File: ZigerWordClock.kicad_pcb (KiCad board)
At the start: 2 copper layers, 237 x 237 mm, 106 parts, among them J1 SAO 1.69bis, J2 Barrel_Jack, U1 BH1750, U10 BTF-5V-060L-B_SK9822_LED_Stri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, U11 BTF-5V-060L-B_SK9822_LED_Stri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, U12 BTF-5V-060L-B_SK9822_LED_Stri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, U13 BTF-5V-060L-B_SK9822_LED_Stri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, U14 BTF-5V-060L-B_SK9822_LED_Stri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, U15 BTF-5V-060L-B_SK9822_LED_Stri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, U16 BTF-5V-060L-B_SK9822_LED_Stri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, U17 BTF-5V-060L-B_SK9822_LED_Stri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, U18 BTF-5V-060L-B_SK9822_LED_Stri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, U19 BTF-5V-060L-B_SK9822_LED_Stri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, U2 LILYGO(R)_TTGO_T8_ESP32-S2_V1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, U20 IR-Module_38KHz, U3 BTF-5V-060L-B_SK9822_LED_Stri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, U4 LevelShifter, U5 BTF-5V-060L-B_SK9822_LED_Stri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, U6 BTF-5V-060L-B_SK9822_LED_Stri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, U7 BTF-5V-060L-B_SK9822_LED_Stri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, U8 BTF-5V-060L-B_SK9822_LED_Stri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, U9 BTF-5V-060L-B_SK9822_LED_Stri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

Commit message: Added silkscreen graphics and version number
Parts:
- added G***: LOGO, WordClock Footprint Library:QR Code ZigerWordClock PCB, B.Cu at (250.7, 59.2)
- added G1: LOGO, WordClock Footprint Library:Schriftzug MiZ, F.Cu at (269.2, 149.6)
- added G2: LOGO, WordClock Footprint Library:Schriftzug Wordclock, F.Cu at (51.6, 149.1)
- added G3: LOGO, WordClock Footprint Library:BackLogo, B.Cu at (153.0, 152.7)
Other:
- board text added: "Infrared Module"
- board text added: "Light Sensor"
- board text added: "Version 1.0"
- board text added: "WiFi LED"

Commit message: Add mounting holes, moved barrel jack, adjusted graphics
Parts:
- added REF**: MountingHole_3.2mm_M3, MountingHole:MountingHole_3.2mm_M3, F.Cu at (274.1, 35.8)
- added REF**: MountingHole_3.2mm_M3, MountingHole:MountingHole_3.2mm_M3, F.Cu at (46.5, 35.8)
- added REF**: MountingHole_3.2mm_M3, MountingHole:MountingHole_3.2mm_M3, F.Cu at (274.6, 263.7)
- added REF**: MountingHole_3.2mm_M3, MountingHole:MountingHole_3.2mm_M3, F.Cu at (46.5, 263.4)
- added REF**: MountingHole_3.2mm_M3, MountingHole:MountingHole_3.2mm_M3, F.Cu at (168.7, 166.4)
- moved J2 31.7 mm to (77.0, 250.9)
- moved G*** 6.47 mm to (246.1, 63.8)
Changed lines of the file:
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@@
     )
   )
-  (footprint "WordClock Footprint Library:Schriftzug Wordclock" (layer "F.Cu")
+  (footprint "MountingHole:MountingHole_3.2mm_M3" locked (layer "F.Cu")
+    (at 274.066 35.814)
+    (descr "Mounting Hole 3.2mm, no annular, M3")
+    (tags "mounting hole 3.2mm no annular m3")
+    (attr exclude_from_pos_files exclude_from_bom)
+    (fp_text reference "REF**" (at 0 -4.2) (layer "F.SilkS") hide
+      (effects (font (size 1 1) (thickness 0.15)))
+    )
+    (fp_text value "MountingHole_3.2mm_M3" (at 0 4.2) (layer "F.Fab")
+      (effects (font (size 1 1) (thickness 0.15)))
+    )
+    (fp_text user "${REFERENCE}" (at 0.3 0) (layer "F.Fab")
+      (effects (font (size 1 1) (thickness 0.15)))
+    )
+    (fp_circle (center 0 0) (end 3.2 0) (layer "Cmts.User") (width 0.15) (fill none))
+    (fp_circle (center 0 0) (end 3.45 0) (layer "F.CrtYd") (width 0.05) (fill none))
+    (pad "" np_thru_hole circle locked (at 0 0) (size 3.2 3.2) (drill 3.2) (layers *.Cu *.Mask))
+  )
+  (footprint "MountingHole:MountingHole_3.2mm_M3" (layer "F.Cu")
+    (at 46.482 35.814)
+    (descr "Mounting Hole 3.2mm, no annular, M3")
+    (tags "mounting hole 3.2mm no annular m3")
+    (attr exclude_from_pos_files exclude_from_bom)
+    (fp_text reference "REF**" (at 0 -4.2) (layer "F.SilkS") hide
+      (effects (font (size 1 1) (thickness 0.15)))
+    )
+    (fp_text value "MountingHole_3.2mm_M3" (at 0 4.2) (layer "F.Fab")
+      (effects (font (size 1 1) (thickness 0.15)))
+    )
+    (fp_text user "${REFERENCE}" (at 0.3 0) (layer "F.Fab")
+      (effects (font (size 1 1) (thickness 0.15)))
+    )
+    (fp_circle (center 0 0) (end 3.2 0) (layer "Cmts.User") (width 0.15) (fill none))
+    (fp_circle (center 0 0) (end 3.45 0) (layer "F.CrtYd") (width 0.05) (fill none))
+    (pad "" np_thru_hole circle locked (at 0 0) (size 3.2 3.2) (drill 3.2) (layers *.Cu *.Mask))
+  )
+  (footprint "WordClock Footprint Library:Schriftzug Wordclock" locked (layer "F.Cu")
     (at 51.562 149.098 -90)
     (attr board_only exclude_from_pos_files exclude_from_bom)
@@
     )
   )
+  (footprint "MountingHole:MountingHole_3.2mm_M3" locked (layer "F.Cu")
+    (at 274.574 263.652)
+    (descr "Mounting Hole 3.2mm, no annular, M3")
+    (tags "mounting hole 3.2mm no annular m3")
+    (attr exclude_from_pos_files exclude_from_bom)
+    (fp_text reference "REF**" (at 0 -4.2) (layer "F.SilkS") hide
+      (effects (font (size 1 1) (thickness 0.15)))
+    )
+    (fp_text value "MountingHole_3.2mm_M3" (at 0 4.2) (layer "F.Fab")
+      (effects (font (size 1 1) (thickness 0.15)))
+    )
+    (fp_text user "${REFERENCE}" (at 0.3 0) (layer "F.Fab")
+      (effects (font (size 1 1) (thickness 0.15)))
+    )
+    (fp_circle (center 0 0) (end 3.2 0) (layer "Cmts.User") (width 0.15) (fill none))
+    (fp_circle (center 0 0) (end 3.45 0) (layer "F.CrtYd") (width 0.05) (fill none))
+    (pad "" np_thru_hole circle locked (at 0 0) (size 3.2 3.2) (drill 3.2) (layers *.Cu *.Mask))
+  )
   (footprint "WordClock Footprint Library:BTF-5V-060L-B SK9822 LED Strip - 11 Segment" locked (layer "F.Cu")
     (at 160.1886 149.5213 180)
@@
     )
   )
+  (footprint "MountingHole:MountingHole_3.2mm_M3" locked (layer "F.Cu")
+    (at 46.482 263.398)
+    (descr "Mounting Hole 3.2mm, no annular, M3")
+    (tags "mounting hole 3.2mm no annular m3")
+    (attr exclude_from_pos_files exclude_from_bom)
+    (fp_text reference "REF**" (at 0 -4.2) (layer "F.SilkS") hide
+      (effects (font (size 1 1) (thickness 0.15)))
+    )
+    (fp_text value "MountingHole_3.2mm_M3" (at 0 4.2) (layer "F.Fab")
+      (effects (font (size 1 1) (thickness 0.15)))
+    )
+    (fp_text user "${REFERENCE}" (at 0.3 0) (layer "F.Fab")
+      (effects (font (size 1 1) (thickness 0.15)))
+    )
+    (fp_circle (center 0 0) (end 3.2 0) (layer "Cmts.User") (width 0.15) (fill none))
+    (fp_circle (center 0 0) (end 3.45 0) (layer "F.CrtYd") (width 0.05) (fill none))
+    (pad "" np_thru_hole circle locked (at 0 0) (size 3.2 3.2) (drill 3.2) (layers *.Cu *.Mask))
+  )
   (footprint "WordClock Footprint Library:BH1750 Breakout Board" locked (layer "F.Cu")
     (at 160.058654 257.18123)
@@
     )
   )
-  (footprint "WordClock Footprint Library:Schriftzug MiZ" (layer "F.Cu")
+  (footprint "WordClock Footprint Library:Schriftzug MiZ" locked (layer "F.Cu")
     (at 269.24 149.606 90)
     (attr board_only exclude_from_pos_files exclude_from_bom)
@@
       ) (layer "F.SilkS") (width 0) (fill solid))
   )
+  (footprint "MountingHole:MountingHole_3.2mm_M3" (layer "F.Cu")
+    (at 168.656 166.36404)
+    (descr "Mounting Hole 3.2mm, no annular, M3")
+    (tags "mounting hole 3.2mm no annular m3")
+    (attr exclude_from_pos_files exclude_from_bom)
+    (fp_text reference "REF**" (at 0 -4.2) (layer "F.SilkS") hide
+      (effects (font (size 1 1) (thickness 0.15)))
+    )
+    (fp_text value "MountingHole_3.2mm_M3" (at 0 4.2) (layer "F.Fab")
+      (effects (font (size 1 1) (thickness 0.15)))
+    )
+    (fp_text user "${REFERENCE}" (at 0.3 0) (layer "F.Fab")
+      (effects (font (size 1 1) (thickness 0.15)))
+    )
+    (fp_circle (center 0 0) (end 3.2 0) (layer "Cmts.User") (width 0.15) (fill none))
+    (fp_circle (center 0 0) (end 3.45 0) (layer "F.CrtYd") (width 0.05) (fill none))
+    (pad "" np_thru_hole circle (at 0 0) (size 3.2 3.2) (drill 3.2) (layers *.Cu *.Mask))
+  )
   (footprint "WordClock Footprint Library:BTF-5V-060L-B SK9822 LED Strip - 11 Segment" locked (layer "F.Cu")
     (at 160.1886 166.36404)
@@
       (net 57 "Net-(JP20-Pad1)") (pinfunction "1") (pintype "passive"))
   )
-  (footprint "WordClock Footprint Library:QR Code ZigerWordClock PCB" (layer "B.Cu")
-    (at 250.698 59.182 180)
+  (footprint "WordClock Footprint Library:QR Code ZigerWordClock PCB" locked (layer "B.Cu")
+    (at 246.126 63.754 180)
     (attr board_only exclude_from_pos_files exclude_from_bom)
     (fp_text reference "G***" (at 0 0) (layer "B.SilkS") hide
@@
       ) (layer "B.SilkS") (width 0) (fill solid))
   )
-  (footprint "WordClock Footprint Library:BackLogo" (layer "B.Cu")
+  (footprint "WordClock Footprint Library:BackLogo" locked (layer "B.Cu")
     (at 153.037186 152.72006 180)
     (attr board_only exclude_from_pos_files exclude_from_bom)
@@
       (primitives
         (gr_poly (pts
-            (xy 0.55 -0.75)
-            (xy 0 -0.75)
-            (xy 0 0.75)
             (xy 0.55 0.75)
+            (xy 0 0.75)
+            (xy 0 -0.75)
+            (xy 0.55 -0.75)
           ) (width 0) (fill yes))
             (gr_circle (center 0 -0.25) (end 0.5 -0.25) (width 0) (fill yes))
@@
         (gr_circle (center 0 0.25) (end 0.5 0.25) (width 0) (fill yes))
         (gr_poly (pts
-            (xy 0 -0.75)
-            (xy -0.55 -0.75)
-            (xy -0.55 0.75)
             (xy 0 0.75)
+            (xy -0.55 0.75)
+            (xy -0.55 -0.75)
+            (xy 0 -0.75)
           ) (width 0) (fill yes))
       ))
@@
   )
   (footprint "Connector_PinHeader_2.54mm:PinHeader_1x02_P2.54mm_Vertical" (layer "B.Cu")
-    (at 47 261.225 180)
+    (at 76.962 250.947 180)
     (descr "Through hole straight pin header, 1x02, 2.54mm pitch, single row")
     (tags "Through hole pin header THT 1x02 2.54mm single row")
@@
       (net 58 "Net-(JP23-Pad1)") (pinfunction "1") (pintype "passive"))
   )
-  (gr_rect (start 34.544 271.272) (end 65.532 245.872) (layer "B.SilkS") (width 0.2) (fill solid))
+  (gr_rect locked (start 34.544 271.272) (end 65.532 245.872) (layer "B.SilkS") (width 0.2) (fill solid))
   (gr_poly
     (pts
@@
       (xy 41.837005 31.032291)
     ) (layer "Edge.Cuts") (width 0.1) (fill none))
-  (gr_text "Infrared Module" (at 118.11 259.842) (layer "F.Cu")
-    (effects (font (size 1.5 1.5) (thickness 0.3)))
-  )
-  (gr_text "Light Sensor" (at 160.02 245.872) (layer "F.Cu")
+  (gr_text "Infrared Module" (at 118.11 259.842) (layer "F.SilkS")
     (effects (font (size 1.5 1.5) (thickness 0.3)))
   )
@@
     (effects (font (size 1.5 1.5) (thickness 0.3)))
   )
+  (gr_text "Light Sensor" (at 160.02 245.872) (layer "F.SilkS")
+    (effects (font (size 1.5 1.5) (thickness 0.3)))
+  )

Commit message: Added JLCPCB DRC Rules
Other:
- rule pad_to_mask_clearance: 0 -> 0.05
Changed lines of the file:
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@@
       (dielectric_constraints no)
     )
-    (pad_to_mask_clearance 0)
+    (pad_to_mask_clearance 0.05)
+    (solder_mask_min_width 0.254)
     (pcbplotparams
       (layerselection 0x00010fc_ffffffff)

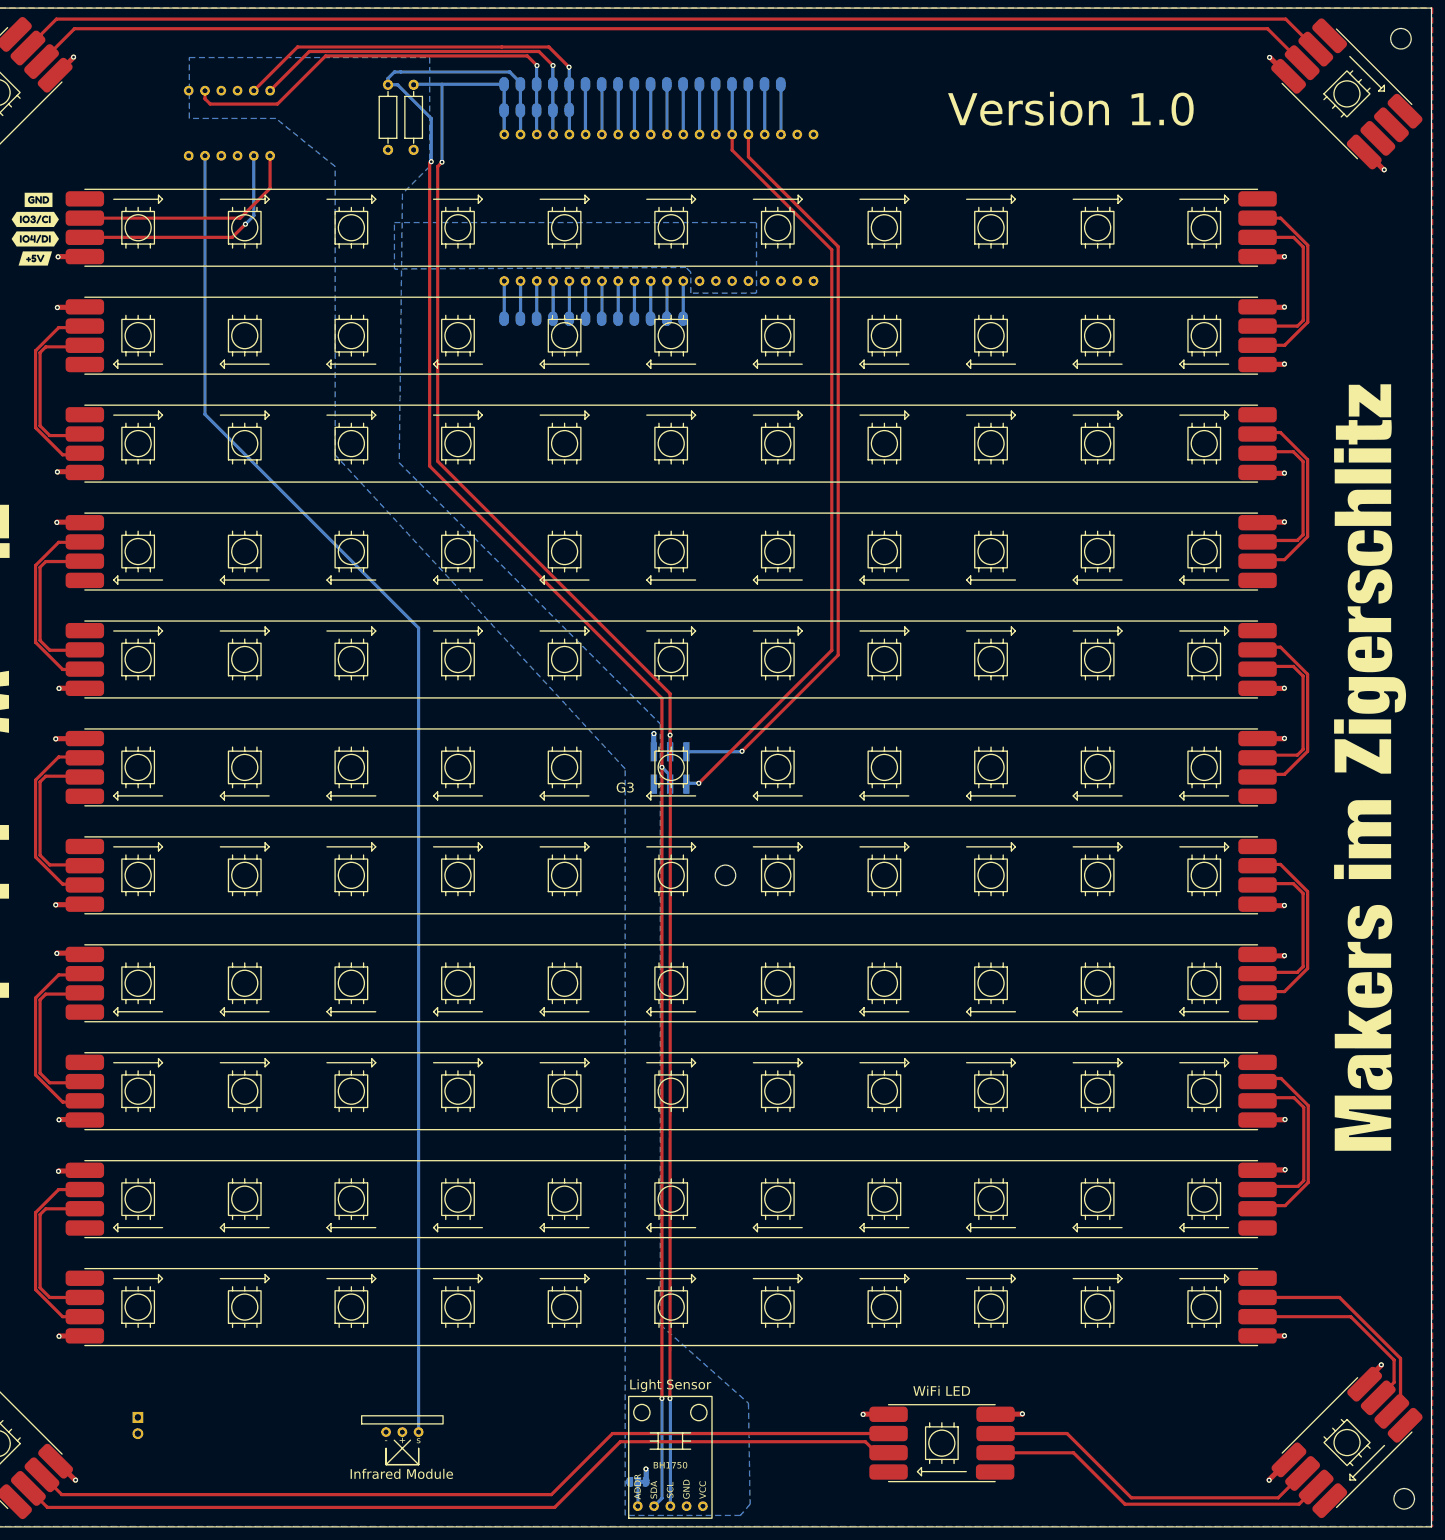
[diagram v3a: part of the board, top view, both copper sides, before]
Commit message: Moved copper traces and created GERBER Files
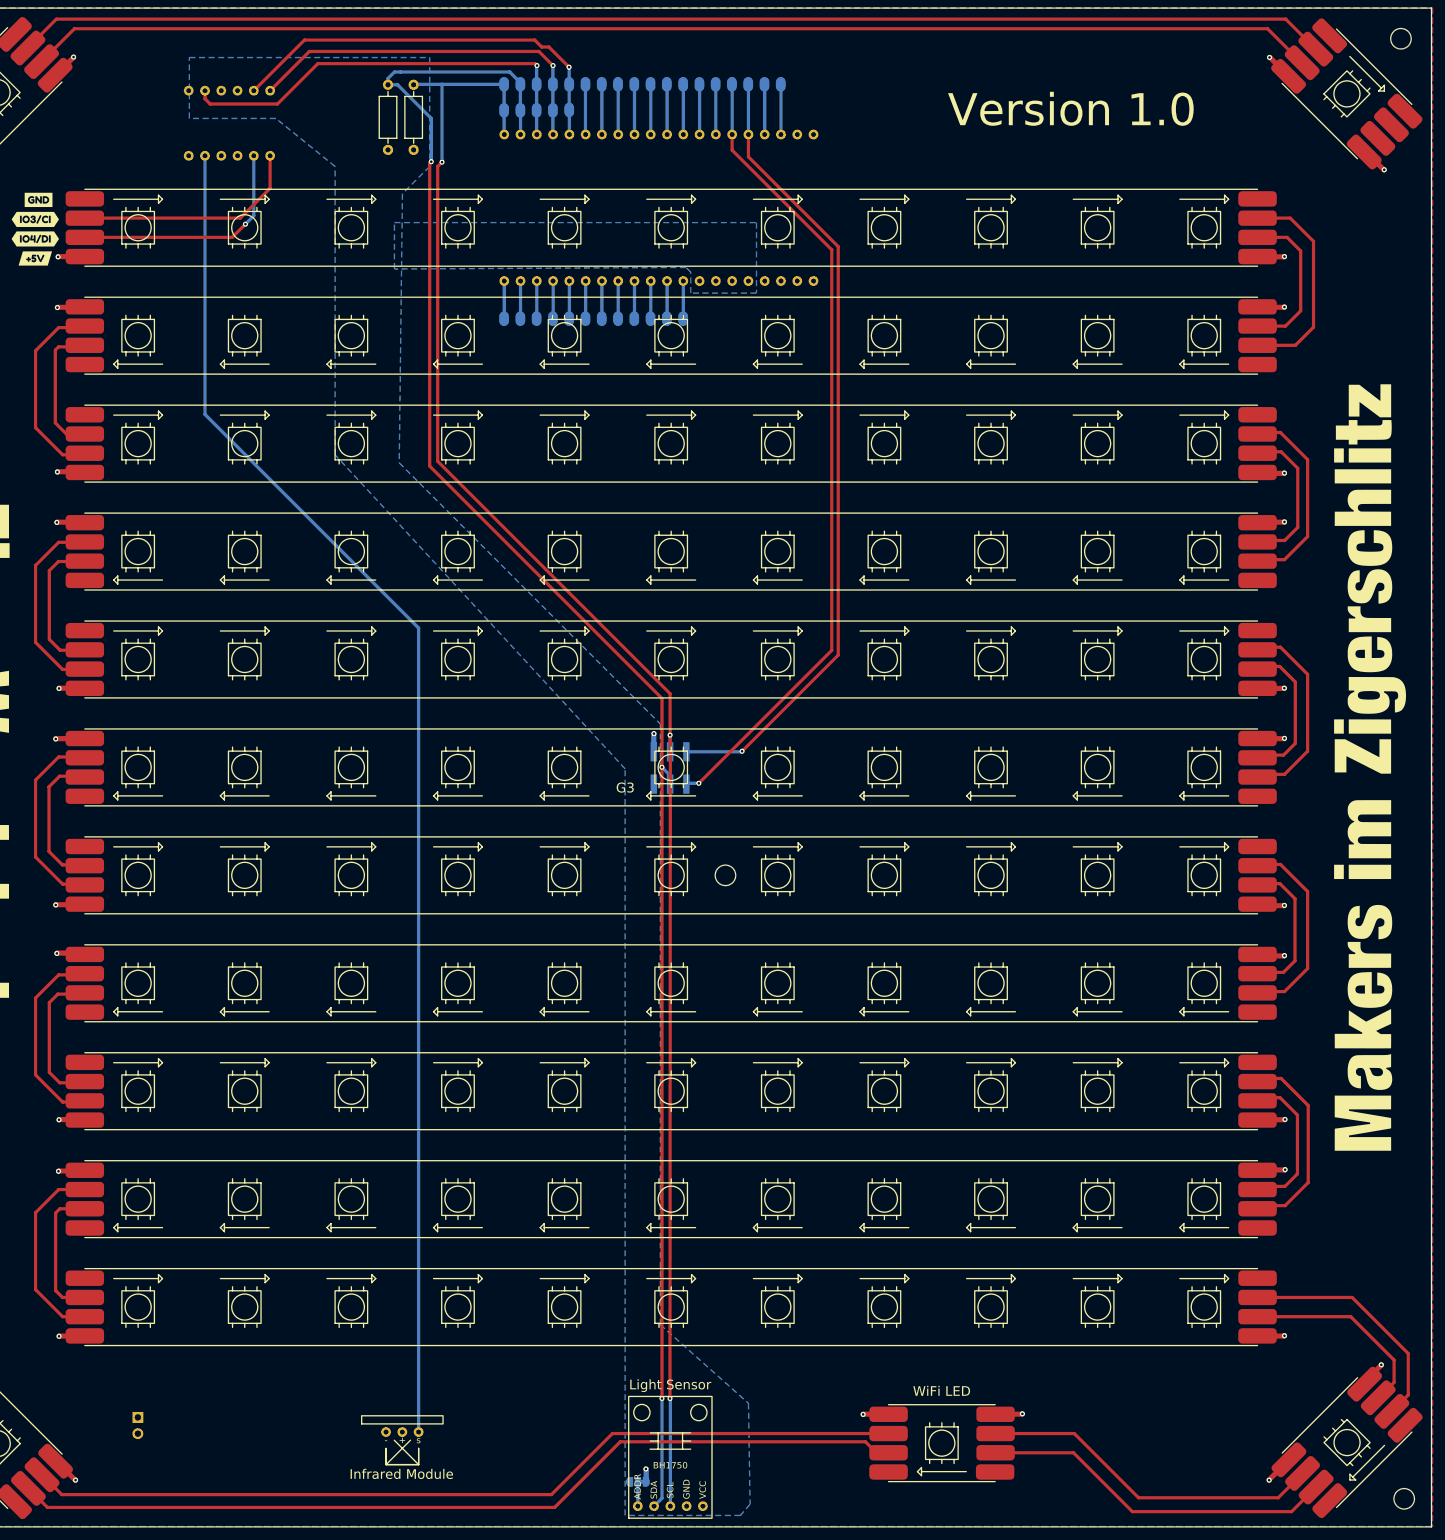
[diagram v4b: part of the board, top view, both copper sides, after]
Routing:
- net Net-(U14-PadCI): track 26.7 -> 21.9 mm
- net Net-(U12-PadCO): track 26.7 -> 22.2 mm
- net GND: track 9.06 -> 4.86 mm, vias 3 -> 2
- net Net-(U10-PadCO): track 26.7 -> 23.1 mm
- net Net-(U11-PadDI): track 26.7 -> 23.2 mm
- net Net-(U10-PadDI): track 26.7 -> 23.2 mm
- net Net-(U15-PadCI): track 26.7 -> 23.4 mm
- net Net-(U12-PadDI): track 26.7 -> 23.4 mm
- net Net-(U11-PadCO): track 26.7 -> 23.5 mm
- net Net-(U14-PadDO): track 26.7 -> 23.7 mm
- net Net-(U13-PadCO): track 30.9 -> 33.5 mm
- net Net-(U18-PadCO): track 35.1 -> 37.2 mm
- net Net-(U13-PadDO): track 26.7 -> 24.7 mm
- net SIG: track 67.9 -> 66.9 mm
- net Net-(U19-PadCO): track 54.5 -> 55.4 mm
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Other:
- rule pad_to_mask_clearance: 0.05 -> 0
